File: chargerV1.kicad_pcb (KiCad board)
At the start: 2 copper layers, 70 x 70 mm, 47 parts, among them J1 USB_C_Receptacle, J2 SOCKET_1x4, J3 SOCKET_1x4, J4 SOCKET_1x6, J5 Micro_SD_Card, SW1 BOOT, SW2 OK, SW3 RESET, SW4 UP, SW5 DW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

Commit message: Add modifies
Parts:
- C14, C15, C16, C17, C24: footprint IVSFootprint:C0603 -> IVS_footprints:C_0603
- J2, J3, SENSOR1: footprint IVSFootprint:SH-1.0mm-1x4 -> IVS_footprints:JST_SH_SM04B-SRSS-TB_1x04-1MP_P1.00mm_Horizontal
- J4: footprint IVSFootprint:SH-1.0mm-1x6 -> IVS_footprints:JST_SH_SM06B-SRSS-TB_1x06-1MP_P1.00mm_Horizontal
- LCD1: footprint IVSFootprint:SH-1.0mm-1x8 -> IVS_footprints:JST_SH_SM08B-SRSS-TB_1x08-1MP_P1.00mm_Horizontal
- SW1, SW3: footprint IVSFootprint:SW_SPST_PTS810 -> IVS_footprints:SW_SPST_PTS810
- SW2, SW4, SW5: footprint IVS_footprints:BUTTON_PUSH_12mm -> IVS_footprints:Button_Push_12mm
- moved LCD1 1.18 mm to (92.4, 125.1)
- moved J4 0.90 mm to (125.2, 120.6)
- moved J1 0.89 mm to (62.5, 95.0)
- moved J2 0.37 mm to (92.6, 89.5)
- moved SENSOR1 0.37 mm to (84.1, 89.5)
- moved C3 0.24 mm to (96.9, 103.5)
- moved R5 0.24 mm to (93.1, 103.5)
- moved C15 0.09 mm to (73.7, 97.0)
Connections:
- J5 pad 10: (no net) -> GND
- LCD1 pad MP: (no net) -> GND
- SENSOR1 pad MP: (no net) -> GND
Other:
- outline, holes or cut-outs redrawn
- board text added: "V2.1"
- board text removed: "V2.0"

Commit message: Add more modifies
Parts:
- C4, C6, C7, C8: footprint IVSFootprint:C0603 -> IVS_footprints:C_0603
- D1: footprint IVSFootprint:D_MiniMELF -> IVS_footprints:D_MiniMELF
- moved R9 2.96 mm to (93.4, 110.9)
- moved J3 2.93 mm to (94.2, 71.8), turned to -90 degrees
- moved C5 2.61 mm to (97.5, 112.0), turned to 180 degrees
- moved G*** 2.03 mm to (82.0, 110.6)
- moved R5 1.78 mm to (94.9, 103.5)
- moved D1 1.65 mm to (110.0, 85.5), turned to 90 degrees
- moved JP1 1.53 mm to (105.8, 87.2)
- moved C3 1.15 mm to (98.0, 103.0), turned to 90 degrees
- moved R6 1.13 mm to (97.5, 110.0), turned to 180 degrees
- moved C4 0.95 mm to (112.7, 86.5)
- moved C6 0.62 mm to (114.6, 86.5)
- moved C7 0.30 mm to (116.5, 86.5)
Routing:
- net /RST: track 86.8 -> 82.9 mm
- net +3.3V: track 256.5 -> 259.6 mm
- net Net-(J3-Pad4): track 31.4 -> 33.8 mm
- net Net-(J3-Pad3): track 17.7 -> 19.9 mm
- net Net-(D1-K): track 16.0 -> 17.4 mm
- net GND: track 15.5 -> 14.1 mm, vias 127 -> 120
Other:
- board text removed: "OK UP DW GND"

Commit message: Add more modifies
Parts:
- removed G***: LOGO, LOGO
- added C10: 10uF, IVS_footprints:C_0603, F.Cu at (87.3, 119.7)
- added REF**: OSHW-Symbol_6.7x6mm_SilkScreen, Symbol:OSHW-Symbol_6.7x6mm_SilkScreen, B.Cu at (115.5, 123.3)
- added REF**: WEEE-Logo_4.2x6mm_SilkScreen, Symbol:WEEE-Logo_4.2x6mm_SilkScreen, B.Cu at (101.8, 123.2)
- added REF**: ESD-Logo_6.6x6mm_SilkScreen, Symbol:ESD-Logo_6.6x6mm_SilkScreen, B.Cu at (107.9, 123.2)
- moved LE1 12.0 mm to (90.2, 96.6), turned to 0 degrees
- moved C15 11.7 mm to (74.7, 85.3), turned to 90 degrees
- moved C14 11.7 mm to (72.9, 85.3), turned to 90 degrees
- moved R4 8.13 mm to (90.1, 99.0), turned to 0 degrees
- moved U4 7.17 mm to (76.8, 91.6)
- moved C1 5.98 mm to (86.5, 106.2), turned to 0 degrees
- moved C2 5.09 mm to (86.5, 108.0), turned to 0 degrees
- moved C17 4.84 mm to (81.3, 96.1), turned to -90 degrees
- moved C16 4.81 mm to (83.2, 96.1), turned to -90 degrees
- moved U1 4.41 mm to (78.5, 106.2)
- moved R1 4.39 mm to (70.4, 103.1)
- moved R2 4.39 mm to (70.4, 109.0)
- moved R3 4.39 mm to (70.4, 111.3)
- moved D2 4.39 mm to (70.2, 106.2)
- moved BT1 3.16 mm to (74.4, 121.1)
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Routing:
- net +3.3V: track 259.6 -> 235.5 mm
- net GND: track 14.1 -> 19.8 mm, vias 120 -> 129
- net VBUS: track 42.5 -> 45.4 mm, vias 6 -> 11
- net +BATT: track 18.2 -> 16.0 mm
- net /BUTT_UP: track 28.7 -> 26.8 mm
- net /BUTT_DW: track 24.8 -> 22.9 mm
- net /BUTT_OK: track 32.8 -> 31.1 mm

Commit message: Fix buttons
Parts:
- removed J2, J3: SOCKET_1x4, IVS_footprints:JST_SH_SM04B-SRSS-TB_1x04-1MP_P1.00mm_Horizontal
- removed SW2: OK, IVS_footprints:Button_Push_12mm
- removed SW4: UP, IVS_footprints:Button_Push_12mm
- removed SW5: DW, IVS_footprints:Button_Push_12mm
- added P1: ~, IVS_footprints:JST_SH_SM05B-SRSS-TB_1x05-1MP_P1.00mm_Horizontal, F.Cu at (94.6, 89.5)
- moved H1 65.0 mm to (127.7, 84.3)
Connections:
- J5 pad 10: GND -> (no net)
- LCD1 pad MP: GND -> (no net)
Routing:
- net Net-(J3-Pad4): track 33.8 -> 0.00 mm, vias 1 -> 0
- net Net-(J3-Pad2): track 28.1 -> 0.00 mm, vias 1 -> 0
- net Net-(J3-Pad3): track 19.9 -> 0.00 mm, vias 1 -> 0
- net GND: track 19.8 -> 6.63 mm, vias 129 -> 112
- net +3.3V: track 235.5 -> 241.9 mm
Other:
- board size 70 x 70 mm -> 70 x 51 mm
- board text removed: "DW"
- board text removed: "OK"
- board text removed: "UP"

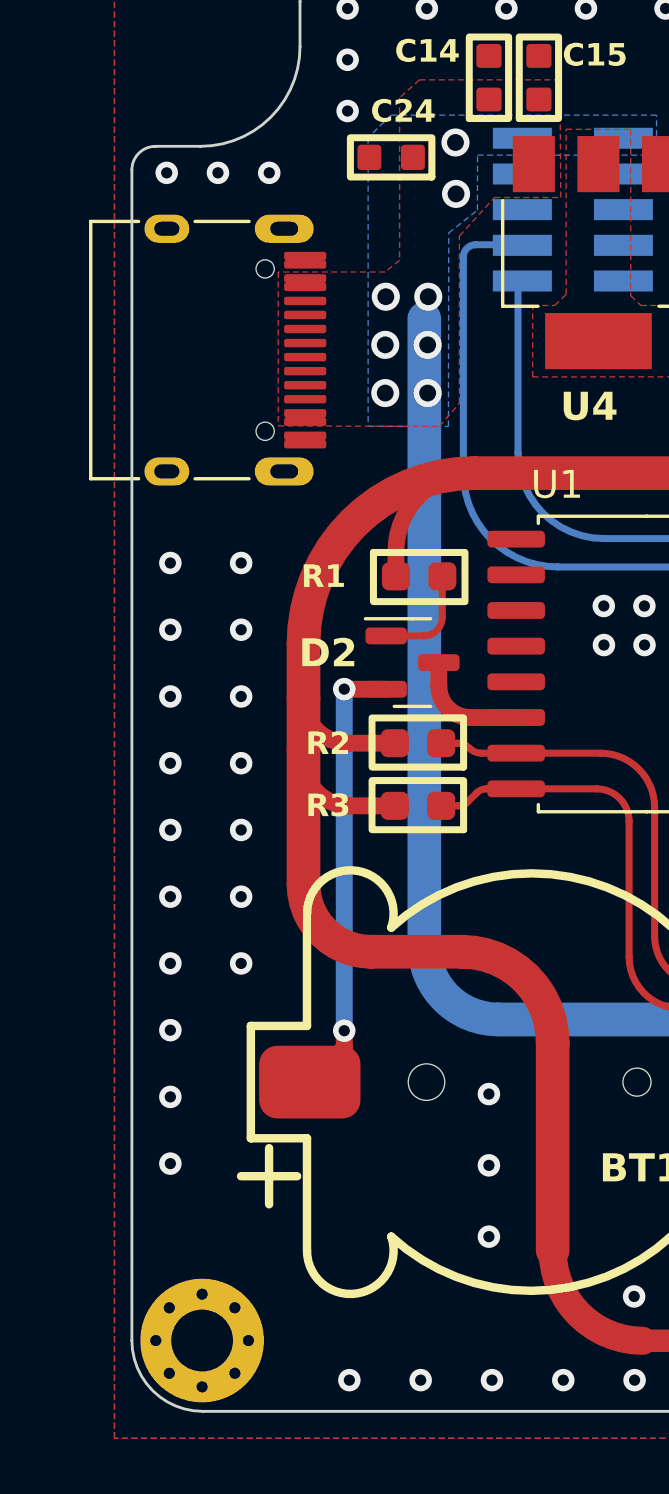
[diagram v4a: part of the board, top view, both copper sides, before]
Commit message: fix usb
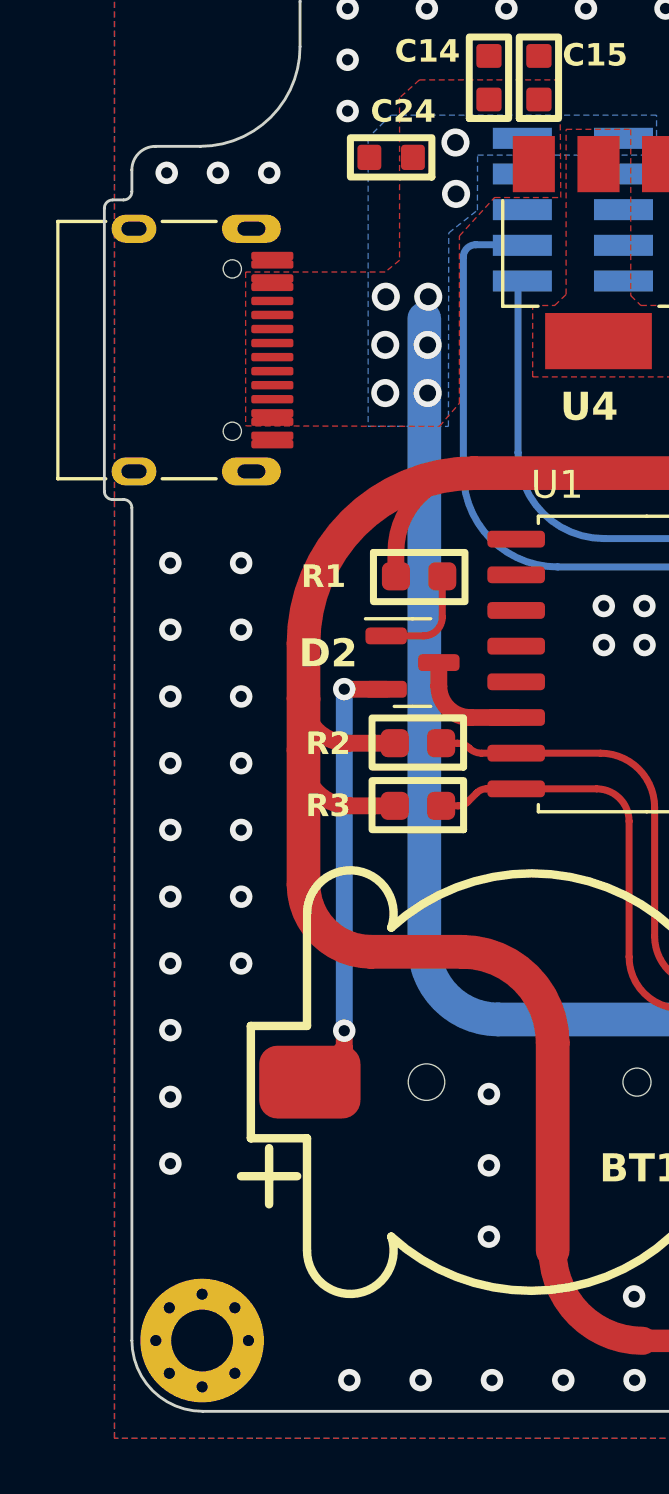
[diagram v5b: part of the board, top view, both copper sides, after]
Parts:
- moved J1 1.17 mm to (61.4, 95.0)
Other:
- board size 70 x 51 mm -> 71 x 51 mm
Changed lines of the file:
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@@
   )
   (footprint "IVS_footprints:USB_C_Receptacle_XKB_U262-16XN-4BVC11" (layer "F.Cu")
-    (at 62.52 95.04 -90)
+    (at 61.35 95.04 -90)
     (descr "USB Type C, right-angle, SMT, https://datasheet.lcsc.com/szlcsc/1811141824_XKB-Enterprise-U262-161N-4BVC11_C319148.pdf")
     (tags "USB C Type-C Receptacle SMD")
@@
     )
   )
-  (gr_line (start 60.2 130.3) (end 60.2 88.63)
+  (gr_arc (start 60.199324 89.4) (mid 60.113051 89.608313) (end 59.904738 89.694586)
+    (stroke (width 0.1) (type default)) (layer "Edge.Cuts"))
+  (gr_line (start 60.2 130.3) (end 60.2 100.66)
     (stroke (width 0.1) (type default)) (layer "Edge.Cuts"))
   (gr_arc (start 62.72 132.82) (mid 60.938091 132.081909) (end 60.2 130.3)
     (stroke (width 0.1) (type default)) (layer "Edge.Cuts"))
+  (gr_line (start 60.199324 89.4) (end 60.199324 88.626949)
+    (stroke (width 0.1) (type default)) (layer "Edge.Cuts"))
   (gr_line (start 130.22 108.83) (end 130.22 130.3)
     (stroke (width 0.1) (type solid)) (layer "Edge.Cuts"))
+  (gr_arc (start 59.904738 100.36) (mid 60.113051 100.446273) (end 60.199324 100.654586)
+    (stroke (width 0.1) (type default)) (layer "Edge.Cuts"))
   (gr_arc (start 130.22 130.3) (mid 129.481909 132.081909) (end 127.7 132.82)
     (stroke (width 0.1) (type default)) (layer "Edge.Cuts"))
@@
   (gr_arc (start 66.186273 82.64) (mid 66.432501 82.045552) (end 67.026949 81.799324)
     (stroke (width 0.1) (type default)) (layer "Edge.Cuts"))
+  (gr_arc (start 59.22 89.99) (mid 59.306273 89.781687) (end 59.514586 89.695414)
+    (stroke (width 0.1) (type default)) (layer "Edge.Cuts"))
+  (gr_line (start 59.904738 89.694586) (end 59.52 89.694586)
+    (stroke (width 0.1) (type default)) (layer "Edge.Cuts"))
   (gr_line (start 62.64 87.786273) (end 61.04 87.786273)
     (stroke (width 0.1) (type default)) (layer "Edge.Cuts"))
+  (gr_arc (start 59.514586 100.36) (mid 59.306273 100.273727) (end 59.22 100.065414)
+    (stroke (width 0.1) (type default)) (layer "Edge.Cuts"))
   (gr_arc (start 127.7 81.8) (mid 129.481897 82.538093) (end 130.22 84.32)
     (stroke (width 0.1) (type default)) (layer "Edge.Cuts"))
   (gr_line (start 123.32625 90.32) (end 123.32625 108.83)
     (stroke (width 0.1) (type solid)) (layer "Edge.Cuts"))
+  (gr_line (start 59.904738 100.36) (end 59.51 100.36)
+    (stroke (width 0.1) (type default)) (layer "Edge.Cuts"))
   (gr_line (start 67.02 81.8) (end 127.7 81.8)
     (stroke (width 0.1) (type solid)) (layer "Edge.Cuts"))
+  (gr_line (start 59.22 100.065414) (end 59.22 89.99)
+    (stroke (width 0.1) (type default)) (layer "Edge.Cuts"))
   (gr_line (start 123.32625 108.83) (end 130.22 108.83)
     (stroke (width 0.1) (type solid)) (layer "Edge.Cuts"))
@@
     (polygon
       (pts
-        (xy 65.41 97.74)
+        (xy 64.25 97.736658)
         (xy 71.146629 97.756532)
         (xy 71.86 96.93387)
@@
         (xy 69.73 91.84)
         (xy 69.22 92.26)
-        (xy 65.41 92.26)
+        (xy 64.25 92.26)
       )
     )
